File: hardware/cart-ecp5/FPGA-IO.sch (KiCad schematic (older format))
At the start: 9 parts, among them J1 JTAG, U1 LFE5U-25F-xBG256x, U2 W25Q128JVSIM, X1 XO_Generic_NC

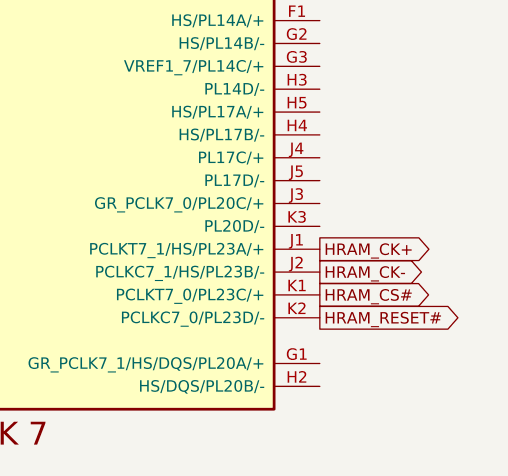
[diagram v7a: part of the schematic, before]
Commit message: Fixes to length matching script, now configured for hyperram
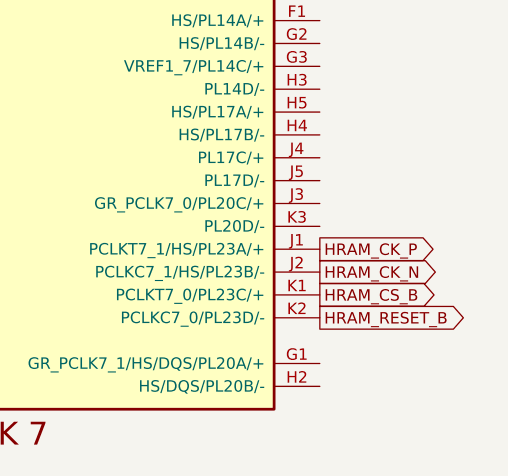
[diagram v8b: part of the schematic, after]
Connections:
- net HRAM_CK+ renamed HRAM_CK_P
- net HRAM_CK- renamed HRAM_CK_N
- net HRAM_CS# renamed HRAM_CS_B
- net HRAM_RESET# renamed HRAM_RESET_B
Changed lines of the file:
@@
 HRAM_RWDS
 Text GLabel 13700 8600 2    50   Output ~ 0
-HRAM_CS#
+HRAM_CS_B
 Text GLabel 13700 8400 2    50   Output ~ 0
-HRAM_CK+
+HRAM_CK_P
 Text GLabel 13700 8500 2    50   Output ~ 0
-HRAM_CK-
+HRAM_CK_N
 Text GLabel 13700 8700 2    50   Output ~ 0
-HRAM_RESET#
+HRAM_RESET_B
 $EndSCHEMATC
